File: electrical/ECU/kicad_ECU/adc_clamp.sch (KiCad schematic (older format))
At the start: 1 part

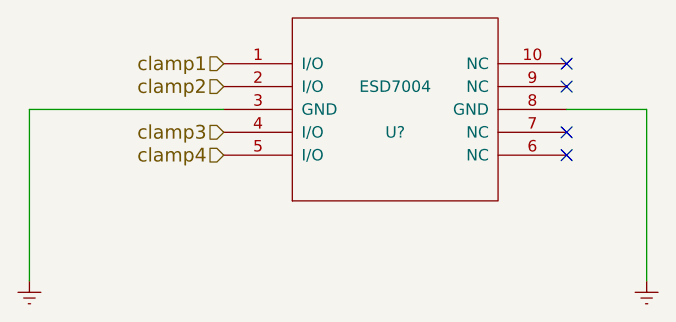
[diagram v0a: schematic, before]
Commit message: fixed some naming errors and initial round of double checking
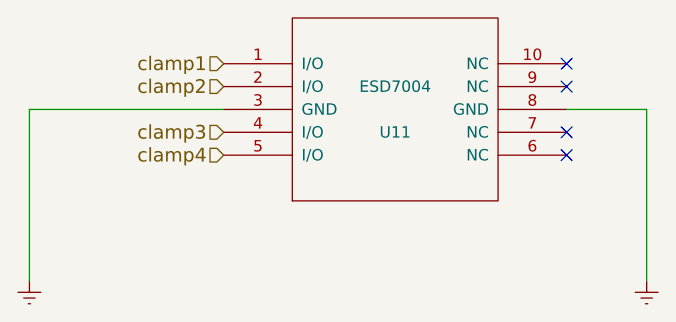
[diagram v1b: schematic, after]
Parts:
- gave numbers to parts that had none: 1
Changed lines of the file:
@@
 $Descr A4 11693 8268
 encoding utf-8
-Sheet 10 33
+Sheet 14 33
 Title "ADC Clamp"
 Date ""
@@
 $EndDescr
 $Comp
-L ESD7004 U?
+L ESD7004 U11
 U 1 1 59774F90
 P 5950 3350
-F 0 "U?" H 5950 3250 50  0000 C CNN
+F 0 "U11" H 5950 3250 50  0000 C CNN
 F 1 "ESD7004" H 5950 3450 50  0000 C CNN
 F 2 "MODULE" H 5950 3350 50  0001 C CNN
@@
 $EndComp
 $Comp
-L Earth #PWR?
+L Earth #PWR42
 U 1 1 59774FB7
 P 7050 4100
-F 0 "#PWR?" H 7050 3850 50  0001 C CNN
+F 0 "#PWR42" H 7050 3850 50  0001 C CNN
 F 1 "Earth" H 7050 3950 50  0001 C CNN
 F 2 "" H 7050 4100 50  0001 C CNN
@@
 $EndComp
 $Comp
-L Earth #PWR?
+L Earth #PWR41
 U 1 1 59774FCD
 P 4350 4100
-F 0 "#PWR?" H 4350 3850 50  0001 C CNN
+F 0 "#PWR41" H 4350 3850 50  0001 C CNN
 F 1 "Earth" H 4350 3950 50  0001 C CNN
 F 2 "" H 4350 4100 50  0001 C CNN
